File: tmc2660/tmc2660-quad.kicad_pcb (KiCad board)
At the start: 4 copper layers, 100 x 50 mm, 83 parts, among them J1 Power, J100 0R, J2 Gadgeteer S, J200 0R, J3 10k, J300 0R, J4 Gadgeteer Y, J400 0R, M0 Mount, M1 Mount, M100 Mount, M101 Mount, M200 Mount, M201 Mount, M300 Mount, M301 Mount, P100 Motor, P200 Motor, P300 Motor, P400 Motor, U100 TMC2660, U200 TMC2660, U300 TMC2660, U400 TMC2660

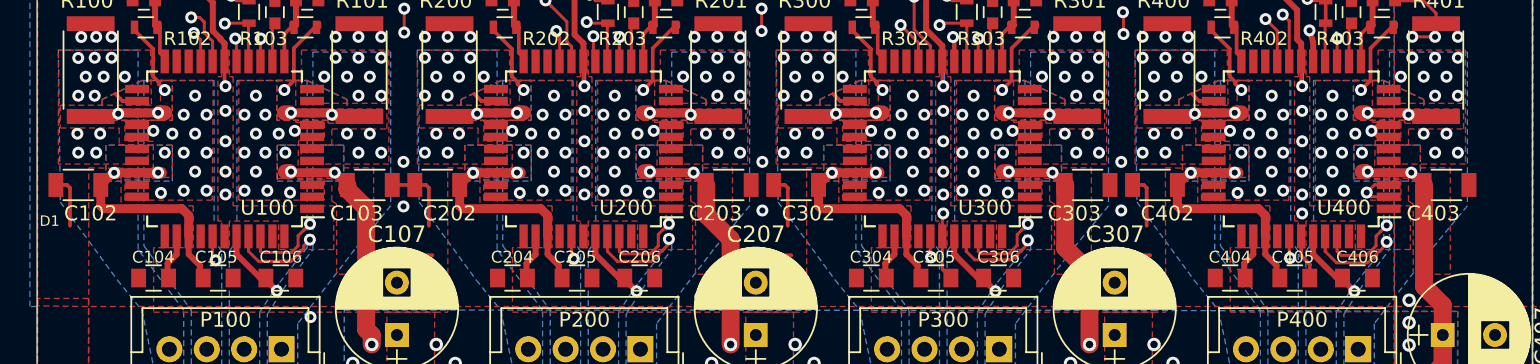
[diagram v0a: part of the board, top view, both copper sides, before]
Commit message: Removed vmot-minipours, uppded BRA/BRB pours priority
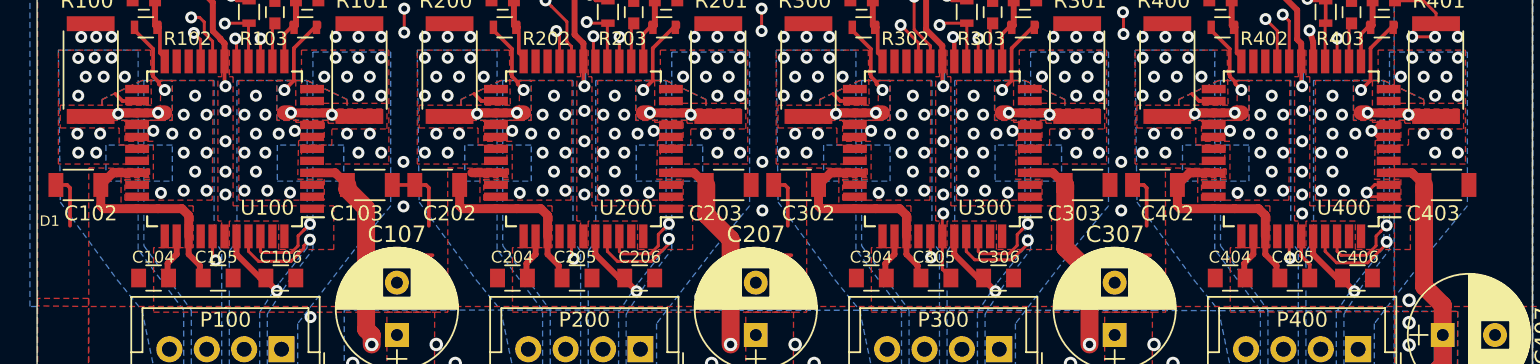
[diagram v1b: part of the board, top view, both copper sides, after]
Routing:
- net VMot: track 145.8 -> 129.2 mm, vias 52 -> 28
- net /TMC2660-100/B2: vias 12 -> 11
